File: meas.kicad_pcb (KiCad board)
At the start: 2 copper layers, 100 x 135 mm, 217 parts, among them J101 Conn_01x06_Socket, J102 Conn_01x02_Socket, J103 Conn_01x02_Socket, J104 Conn_01x02_Socket, J105 Conn_01x02_Socket, Q1001 DPLS350E, U1001 MC7805, U1101 R05C05TE05S, U1201 R05C05TE05S, U1301 R05C05TE05S, U1401 R05C05TE05S, U201 Si8641BD-B-IS2, U301 Si8641BD-B-IS2, U401 Si8641BD-B-IS2, U501 Si8641BD-B-IS2, U601 ADS8665IPWR, U701 ADS8665IPWR, U801 ADS8665IPWR, U901 ACS730xLCTR-20AB

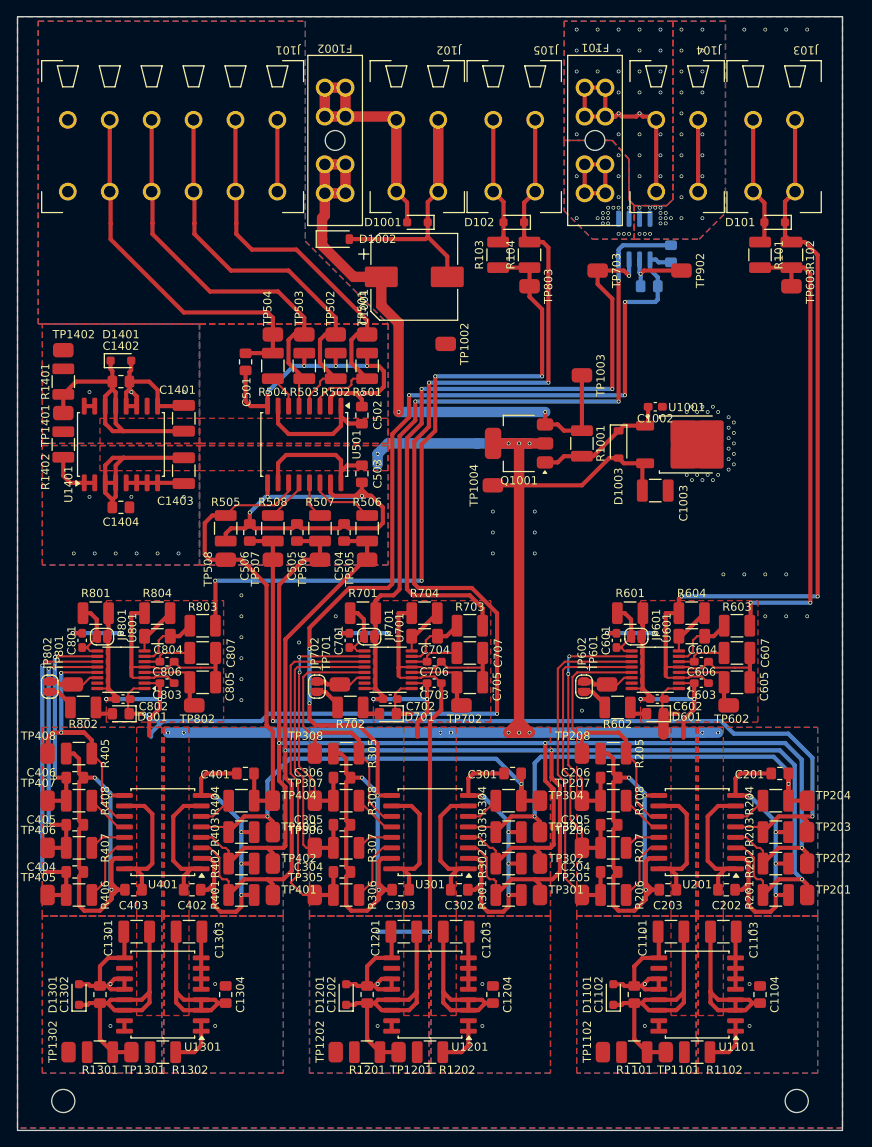
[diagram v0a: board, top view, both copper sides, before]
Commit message: edit silkscreen
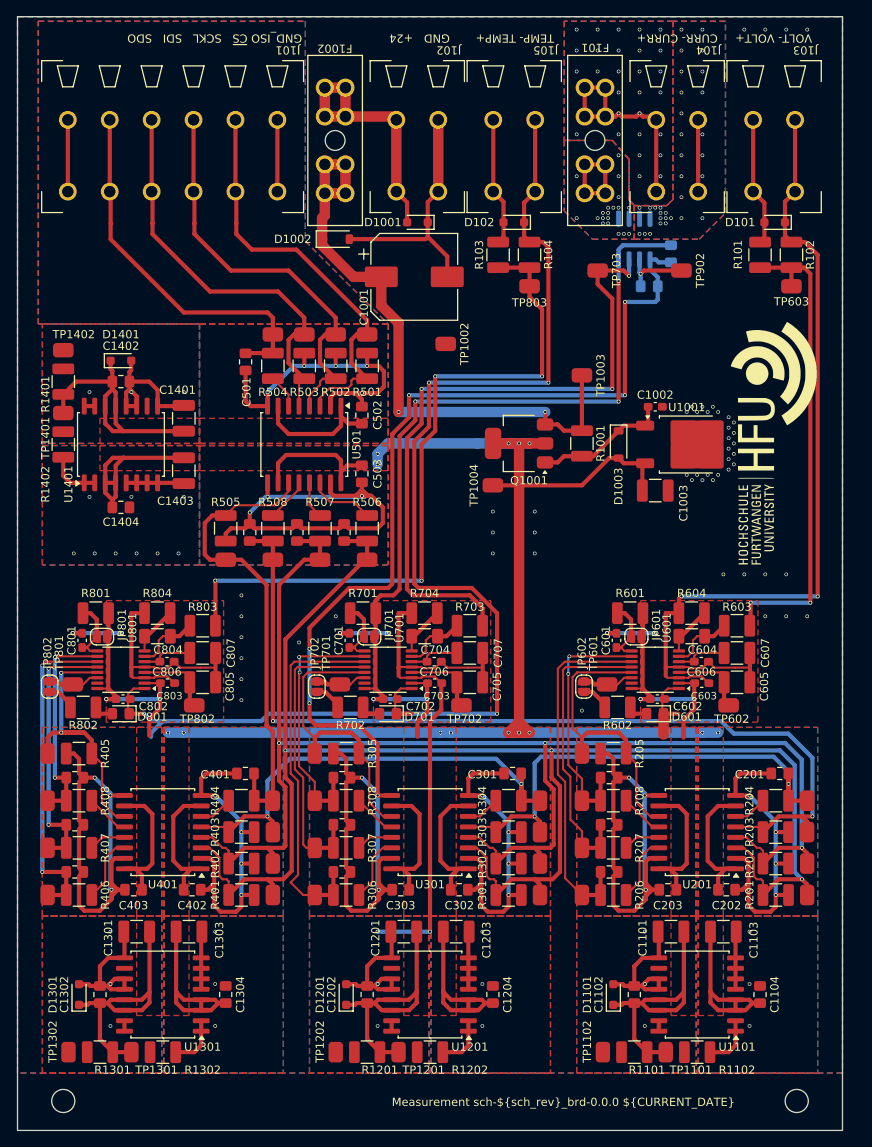
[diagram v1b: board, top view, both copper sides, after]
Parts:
- added G***: LOGO, meas:hfu-logo, F.Cu at (241.7, 91.7)
- REF** (x2): footprint pss:MountingHole_2.8mm -> meas:MountingHole_2.8mm
- moved C603 0.05 mm to (232.9, 120.8)
- moved C803 0.05 mm to (168.2, 120.8)
- moved C703 0.05 mm to (200.6, 120.8)
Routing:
- net unconnected-(J101-Pin_6-Pad6): track 0.00 -> 8.70 mm
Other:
- board text added: "${TITLE} sch-${sch_rev}_brd-${REVISION} ${CURRENT_DATE}"
- board text added: "CURR- CURR+"
- board text added: "GND +24"
- board text added: "GND_ISO ~{CS} SCKL SDI SDO"
- board text added: "TEMP- TEMP+"
- board text added: "VOLT- VOLT+"
